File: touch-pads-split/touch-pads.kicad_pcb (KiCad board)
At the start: 2 copper layers, 120 x 138.2 mm, 19 parts, among them J1 Conn_01x06_Socket, J2 Conn_01x06_Socket, K1 Conn_01x01, K2 Conn_01x01, K3 Conn_01x01, K4 Conn_01x01, K5 Conn_01x01, K6 Conn_01x01, K7 Conn_01x01, K8 Conn_01x01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

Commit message: tweaks to split
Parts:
- removed R3: 150k, Resistor_SMD:R_0805_2012Metric_Pad1.20x1.40mm_HandSolder
- added R2: 150k, Resistor_SMD:R_0805_2012Metric_Pad1.20x1.40mm_HandSolder, F.Cu at (130.5, 253.0)
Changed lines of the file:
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@@
 		(descr "Resistor SMD 0805 (2012 Metric), square (rectangular) end terminal, IPC_7351 nominal with elongated pad for handsoldering. (Body size source: IPC-SM-782 page 72, https://www.pcb-3d.com/wordpress/wp-content/uploads/ipc-sm-782a_amendment_1_and_2.pdf), generated with kicad-footprint-generator")
 		(tags "resistor handsolder")
-		(property "Reference" "R3"
-			(at 0 -1.75 0)
-			(unlocked yes)
+		(property "Reference" "R2"
+			(at 0 -1.65 360)
 			(layer "F.SilkS")
 			(effects
@@
 		)
 		(property "Value" "150k"
-			(at 0 1.65 0)
+			(at 0 1.65 360)
 			(layer "F.Fab")
 			(effects
@@
 		)
 		(fp_text user "${REFERENCE}"
-			(at 0 0 0)
+			(at 0 0 360)
 			(layer "F.Fab")
 			(effects

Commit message: angled jst
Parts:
- J1, J2: footprint Connector_JST:JST_XH_B6B-XH-A_1x06_P2.50mm_Vertical -> Connector_JST:JST_GH_SM06B-GHS-TB_1x06-1MP_P1.25mm_Horizontal
- moved J1 6.25 mm to (88.8, 256.5), turned to 90 degrees
- moved J2 6.25 mm to (148.8, 256.5), turned to -90 degrees
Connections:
- J2 pad 1: SMCLK -> ALERT
- J2 pad 2: SMDATA -> GND
- J2 pad 3: RESET -> +3.3V
- J2 pad 4: +3.3V -> RESET
- J2 pad 5: GND -> SMDATA
- J2 pad 6: ALERT -> SMCLK
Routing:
- net +3.3V: track 77.2 -> 65.5 mm
- net ALERT: track 71.1 -> 60.4 mm
- net GND: track 95.3 -> 84.6 mm
- net RESET: track 69.4 -> 59.3 mm
- net SMDATA: track 68.9 -> 59.1 mm
- net SMCLK: track 69.3 -> 59.9 mm
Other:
- board text added: "ALERT GND +3.3V RESET SMDATA SMCLK"

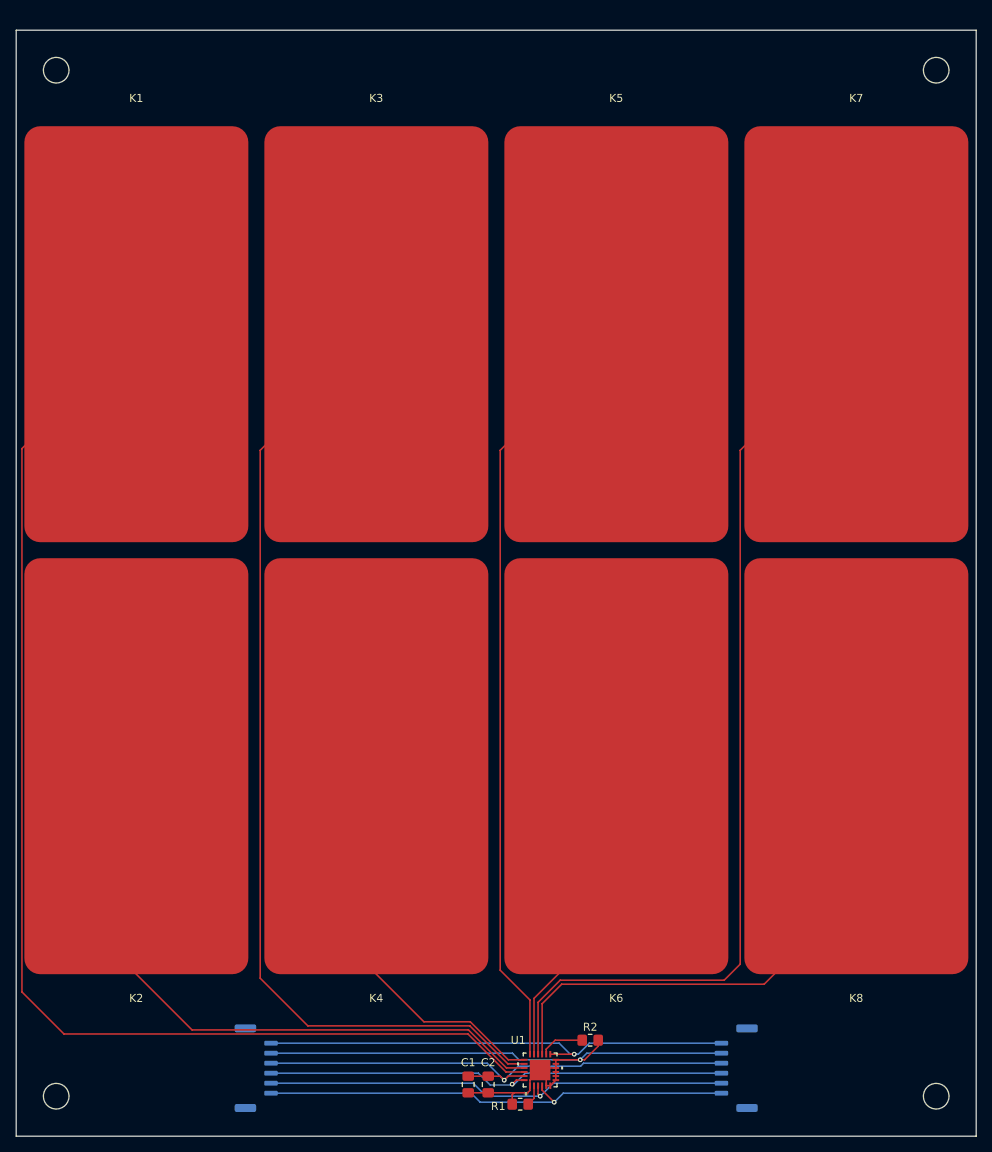
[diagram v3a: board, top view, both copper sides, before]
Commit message: align between two pcbs
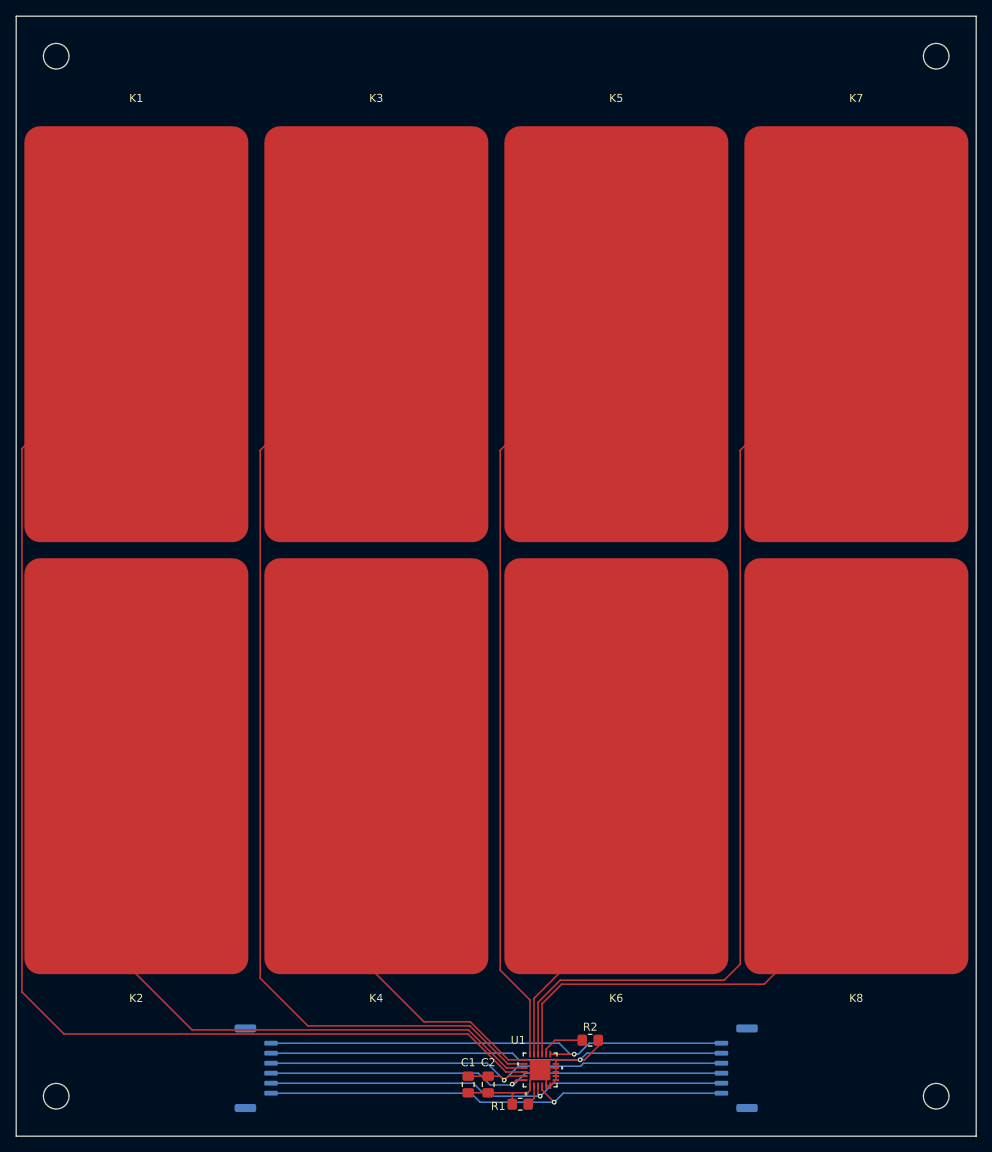
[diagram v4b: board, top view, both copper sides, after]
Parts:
- moved H1 1.75 mm to (63.8, 130.0)
- moved H2 1.75 mm to (173.8, 130.0)
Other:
- board size 120 x 138.2 mm -> 120 x 140 mm
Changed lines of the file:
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@@
 	(footprint "MountingHole:MountingHole_3.2mm_M3"
 		(layer "F.Cu")
-		(at 173.75 131.75)
+		(at 173.75 130)
 		(descr "Mounting Hole 3.2mm, no annular, M3")
 		(tags "mounting hole 3.2mm no annular m3")
@@
 	(footprint "MountingHole:MountingHole_3.2mm_M3"
 		(layer "F.Cu")
-		(at 63.75 131.75)
+		(at 63.75 130)
 		(descr "Mounting Hole 3.2mm, no annular, M3")
 		(tags "mounting hole 3.2mm no annular m3")
@@
 	)
 	(gr_line
-		(start 63.75 126.75)
-		(end 63.75 131.75)
+		(start 63.75 125)
+		(end 63.75 130)
 		(stroke
 			(width 0.1)
@@
 	)
 	(gr_line
-		(start 178.75 131.75)
-		(end 173.75 131.75)
+		(start 178.75 130)
+		(end 173.75 130)
 		(stroke
 			(width 0.1)
@@
 	)
 	(gr_line
-		(start 63.75 131.75)
-		(end 58.75 131.75)
+		(start 63.75 130)
+		(end 58.75 130)
 		(stroke
 			(width 0.1)
@@
 	)
 	(gr_line
-		(start 173.75 131.75)
-		(end 173.75 126.75)
+		(start 173.75 130)
+		(end 173.75 125)
 		(stroke
 			(width 0.1)
@@
 	)
 	(gr_rect
-		(start 58.75 126.75)
+		(start 58.75 125)
 		(end 178.75 265)
 		(stroke
